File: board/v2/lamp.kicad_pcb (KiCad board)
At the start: 4 copper layers, 24 x 24 mm, 44 parts, among them J1 Conn_01x01_Female, J2 Conn_01x01_Female, J3 Conn_01x01_Female, J4 Conn_01x01_Female, J5 Conn_01x01_Female, J6 Conn_01x01_Female, J7 Conn_01x01_Female, U1 STM32F030F4P6, U2 LMV321, U3 MIC5205-3.3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

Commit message: hardware: Various fixes
* Fix component values
* Replace MIC5202 which wasn't ceramic-stable
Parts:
- R11: value 22k -> 8.2k
- R12: value 4.7k -> 2.2k
- R5: value 100k -> 120k
- R9: value 50k -> 10k
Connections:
- net Net-(TP1-Pad1) renamed /RESET
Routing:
- net Net-(R11-Pad2): track 12.5 -> 2.64 mm, vias 2 -> 0
- net /PWRGD: track 9.03 -> 0.00 mm, vias 2 -> 0
- net Net-(U1-Pad18): track 0.00 -> 7.06 mm
- net /RESET: track 5.54 -> 9.03 mm, vias 0 -> 2
- net /VBAT: track 8.99 -> 12.5 mm, vias 1 -> 2
- net Net-(D1-Pad2): track 2.18 -> 5.62 mm
- net Net-(R4-Pad2): track 5.81 -> 8.99 mm
- net Net-(C10-Pad1): track 2.64 -> 0.00 mm
- net Net-(R9-Pad2): track 8.17 -> 5.81 mm
- net Net-(U1-Pad2): track 0.00 -> 1.83 mm
- net Net-(C16-Pad1): track 7.06 -> 8.17 mm, vias 0 -> 1
- net Net-(C7-Pad1): track 1.83 -> 2.87 mm
- net Net-(J4-Pad1): track 2.87 -> 2.18 mm

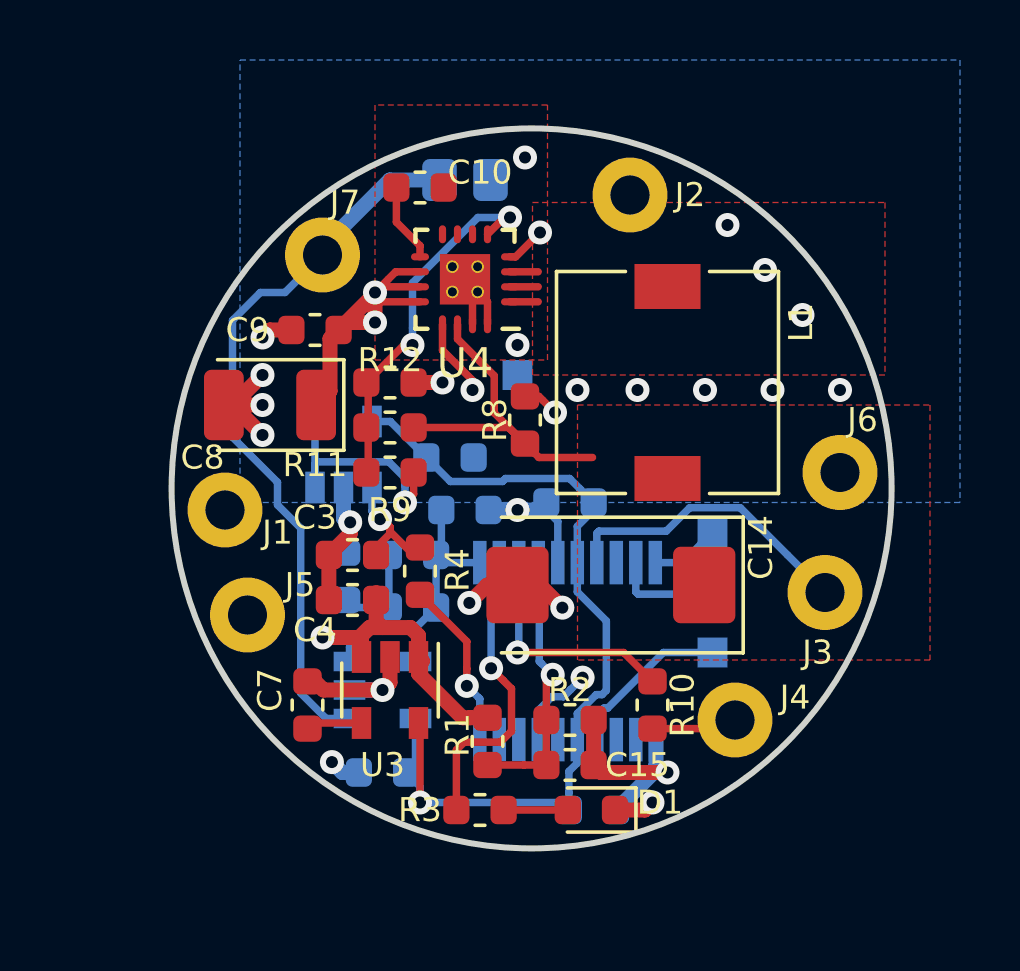
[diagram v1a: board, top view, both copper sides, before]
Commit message: board/v2: Various design changes
 * Switch from MIC5202 to LP2985 due to ceramic stability issues
   with former

 * Use TLV333 for op-amps for reduced power and offset

 * Move current sense amplifier next to sense resistor
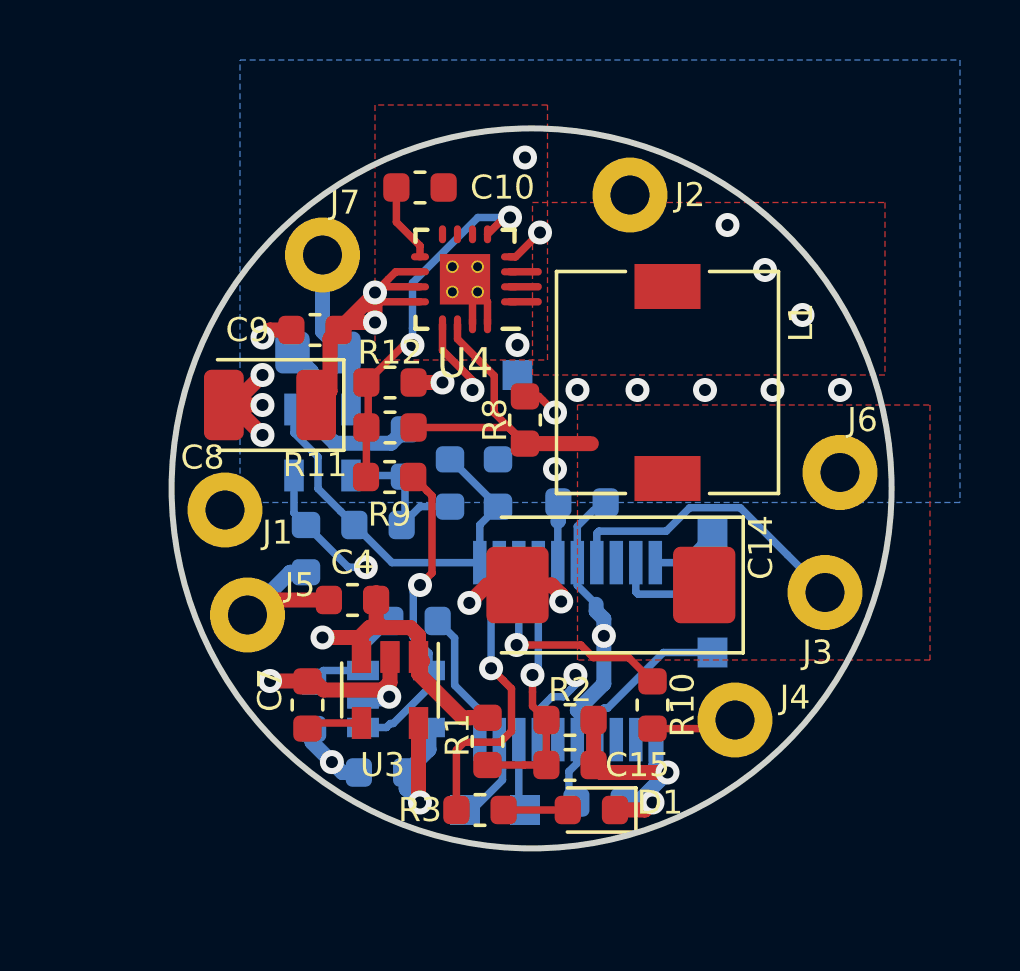
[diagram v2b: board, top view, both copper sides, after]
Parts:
- added TP5: Test_Point, TestPoint:TestPoint_Pad_1.0x1.0mm, B.Cu at (135.5, 94.5)
- added TP6: Test_Point, TestPoint:TestPoint_Pad_1.0x1.0mm, B.Cu at (133.5, 94.5)
- C3: value 1u -> 100n; moved to B.Cu
- C4: value 100n -> 4.7u
- C5: value 2.2u -> 4.7u
- C7: value 100n -> 470p
- R4: moved to B.Cu
- R5: value 120k -> 100k
- U2, U5: value LMV321 -> TLV333
- U3: value MIC5205-3.3 -> LP2985-33
- moved U2 8.49 mm to (128.8, 82.2), turned to 270 degrees
- moved U5 8.34 mm to (131.2, 90.8), turned to 0 degrees
- moved R13 7.55 mm to (128.6, 79.2), turned to 180 degrees
- moved C11 5.68 mm to (128.2, 85.8), turned to 270 degrees
- moved C3 5.19 mm to (128.4, 91.0), turned to 270 degrees
- moved R6 4.56 mm to (131.5, 82.6)
- moved R5 4.33 mm to (133.0, 83.6), turned to 90 degrees
- moved R4 1.67 mm to (131.8, 88.2), turned to 0 degrees
- moved C6 1.52 mm to (130.6, 85.0), turned to 180 degrees
- moved C16 1.42 mm to (134.6, 83.6), turned to 90 degrees
- moved C2 0.40 mm to (137.4, 84.2)
- moved C1 0.35 mm to (138.0, 94.2)
- moved R9 0.15 mm to (131.0, 83.4)
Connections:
- U1 pad 8: Net-(U1-Pad8) -> /DEBUG_TX
- U1 pad 9: Net-(U1-Pad9) -> /DEBUG_RX
- U2 pad 1: /ISENSE -> Net-(C16-Pad1)
- U2 pad 3: Net-(C6-Pad1) -> /ISENSE
- U2 pad 4: Net-(C16-Pad1) -> Net-(C6-Pad1)
- U5 pad 1: /SETPOINT -> Net-(R9-Pad2)
- U5 pad 3: Net-(R9-Pad2) -> /SETPOINT
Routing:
- net /ISENSE: track 24.4 -> 5.58 mm
- net Net-(R11-Pad2): track 2.64 -> 12.6 mm, vias 0 -> 2
- net +3V3: track 31.5 -> 41.3 mm, vias 1 -> 3
- net /PWRGD: track 0.00 -> 9.03 mm, vias 0 -> 2
- net Net-(U1-Pad18): track 7.06 -> 0.00 mm
- net GND: track 37.0 -> 43.4 mm
- net Net-(C16-Pad1): track 8.17 -> 13.9 mm, vias 1 -> 0
- net Net-(R9-Pad2): track 5.81 -> 10.8 mm
- net Net-(R4-Pad2): track 8.99 -> 4.65 mm, vias 1 -> 0
- net /VBAT: track 12.5 -> 8.98 mm, vias 2 -> 1
- net /RESET: track 9.03 -> 5.54 mm, vias 2 -> 0
- net Net-(D1-Pad2): track 5.62 -> 2.18 mm
- net /DEBUG_RX: track 0.00 -> 3.05 mm
- net Net-(C10-Pad1): track 0.00 -> 2.64 mm
- net /DEBUG_TX: track 0.00 -> 2.43 mm
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- added copper zone on In2.Cu, net GND

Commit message: board/v2: Use two-channel op-amp
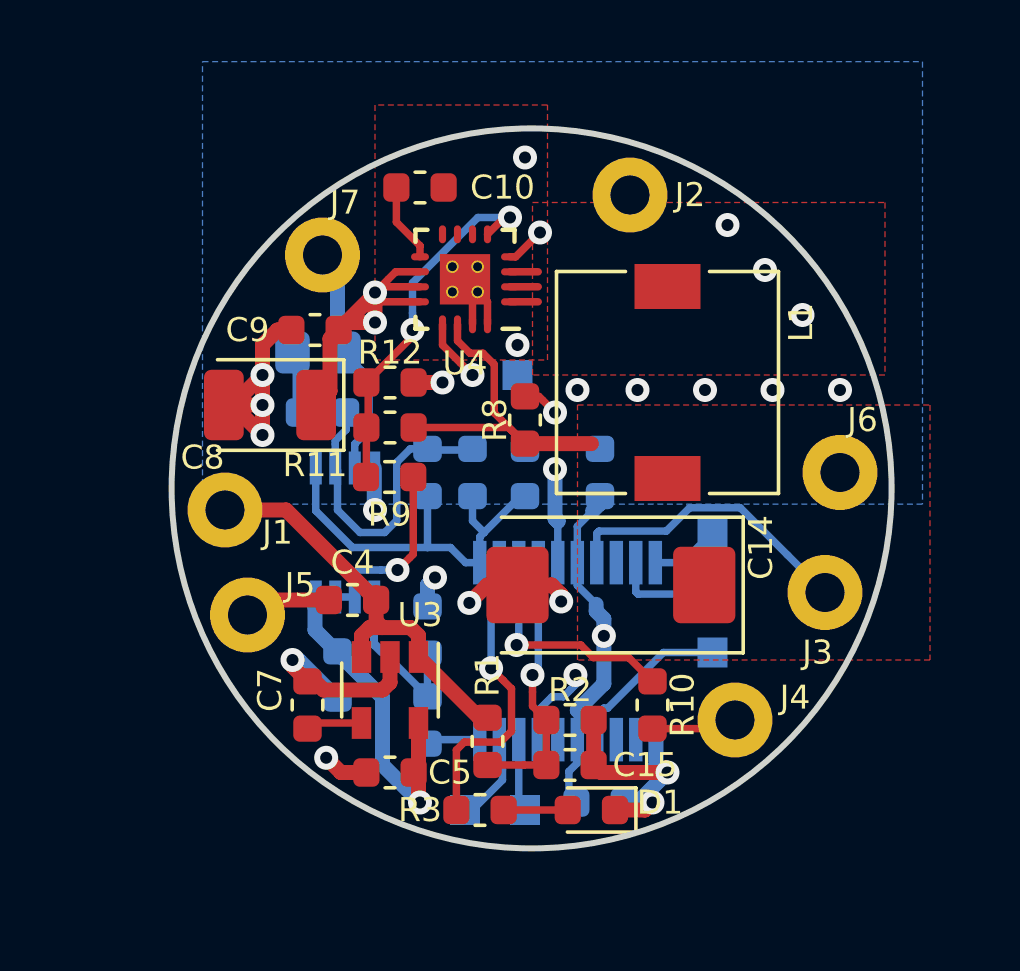
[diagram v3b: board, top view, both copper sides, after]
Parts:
- removed U5: TLV333, Package_TO_SOT_SMD:SOT-23-5
- C10: value 3.3n -> 4.7n
- C5: moved to F.Cu
- C7: value 470p -> 10n
- U2: value TLV333 -> TLV2333; footprint Package_TO_SOT_SMD:SOT-23-5 -> Package_SO:TSSOP-8_3x3mm_P0.65mm
- moved C3 4.60 mm to (132.2, 88.5), turned to 90 degrees
- moved C11 4.34 mm to (129.2, 90.0)
- moved R4 3.33 mm to (132.2, 91.5), turned to 270 degrees
- moved U2 3.09 mm to (129.5, 85.2)
- moved R6 3.06 mm to (128.8, 81.2), turned to 0 degrees
- moved C6 2.41 mm to (132.2, 83.2), turned to 270 degrees
- moved C2 1.17 mm to (138.0, 83.2), turned to 90 degrees
- moved C16 0.97 mm to (135.5, 83.2)
- moved R5 0.83 mm to (133.8, 83.2), turned to 270 degrees
- moved C5 0.25 mm to (131.0, 93.2)
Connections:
- U2 pad 2: GND -> Net-(C6-Pad1)
- U2 pad 4: Net-(C6-Pad1) -> GND
- U2 pad 5: +3V3 -> /SETPOINT
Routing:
- net +3V3: track 41.3 -> 33.8 mm, vias 3 -> 2
- net Net-(C6-Pad1): track 5.34 -> 10.5 mm
- net Net-(R9-Pad2): track 10.8 -> 6.23 mm
- net /VIN: track 22.7 -> 26.8 mm, vias 3 -> 2
- net /SETPOINT: track 3.88 -> 7.02 mm
- net /ISENSE: track 5.58 -> 7.98 mm
- net Net-(R4-Pad2): track 4.65 -> 2.41 mm
- net GND: track 43.4 -> 44.4 mm

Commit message: Hardware changes
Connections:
- net Net-(C16-Pad1) renamed /ISENSE_BUFD
- net Net-(R4-Pad2) renamed /SETPOINT_PWM

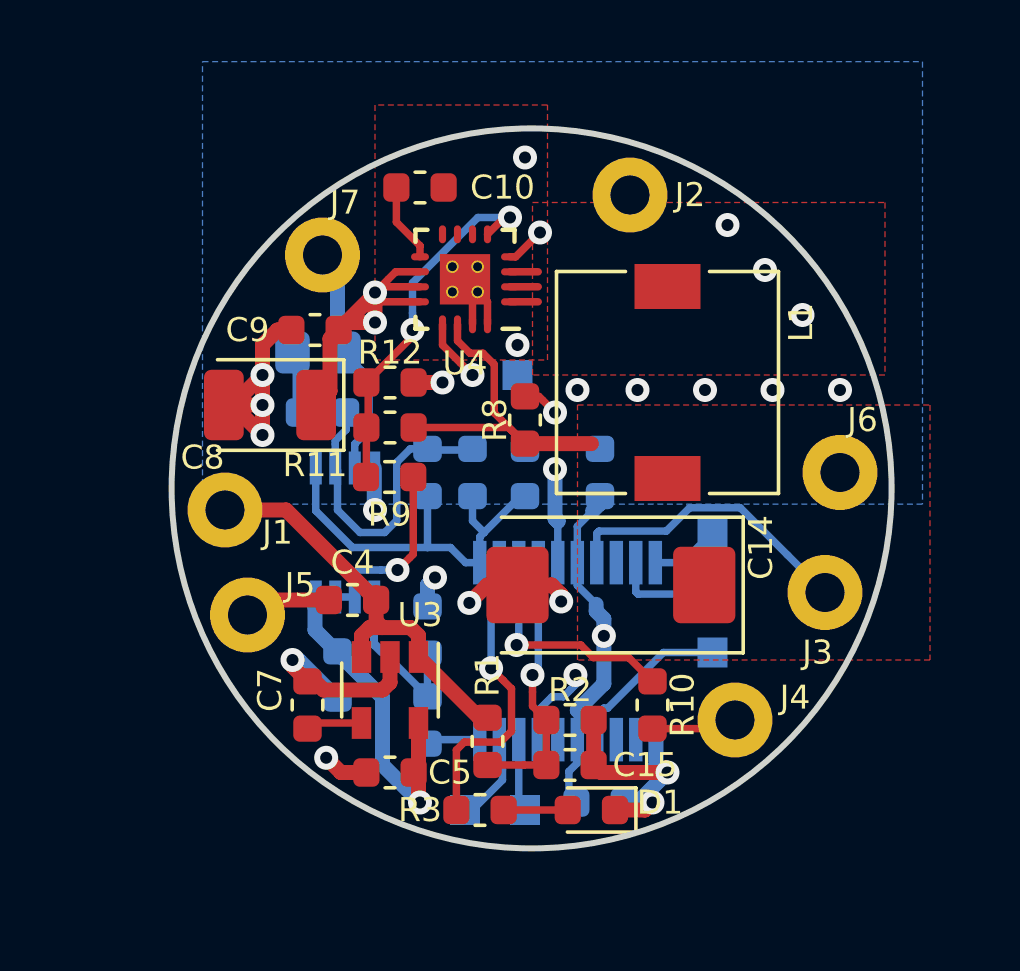
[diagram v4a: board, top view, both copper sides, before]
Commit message: board/v2: Move to STM32L041F6P7
This required only a small change in pinning which can be easily bodged
onto the existing boards.
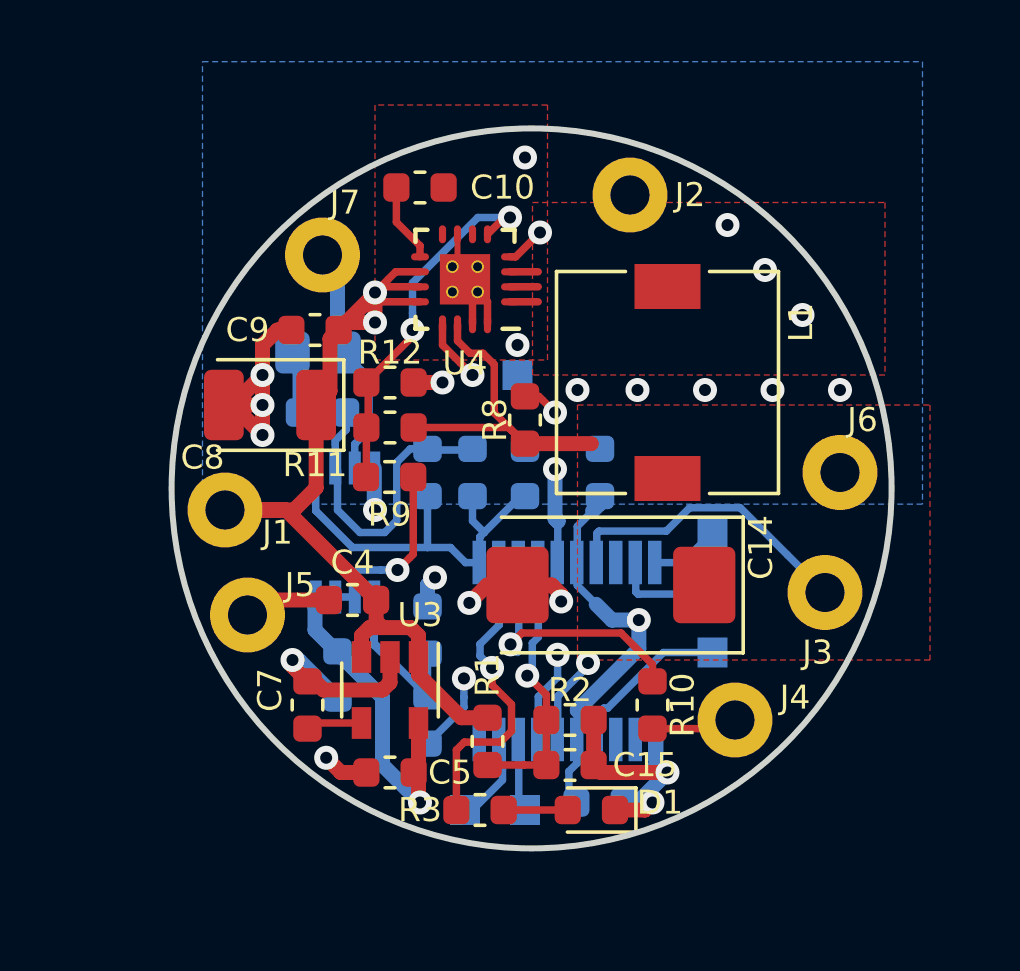
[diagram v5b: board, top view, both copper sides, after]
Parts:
- U1: value STM32F030F4P6 -> STM32L041F6Px
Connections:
- U1 pad 10: /SETPOINT_PWM -> Net-(U1-Pad10)
- U1 pad 6: Net-(U1-Pad6) -> /SETPOINT_PWM
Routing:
- net /SETPOINT_PWM: track 2.41 -> 10.6 mm, vias 0 -> 2
- net /VIN: track 26.8 -> 33.2 mm
- net +3V3: track 33.8 -> 37.5 mm
- net GND: track 44.4 -> 45.5 mm
- net /EN: track 16.7 -> 15.7 mm
- net /LED2: track 8.09 -> 9.09 mm
- net Net-(U1-Pad10): track 0.00 -> 0.61 mm
- added copper zone on In1.Cu, net /VIN
- removed copper zone on In2.Cu, net /VIN

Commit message: hardware: Kicad update
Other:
- net class Default removed
- net class Power removed

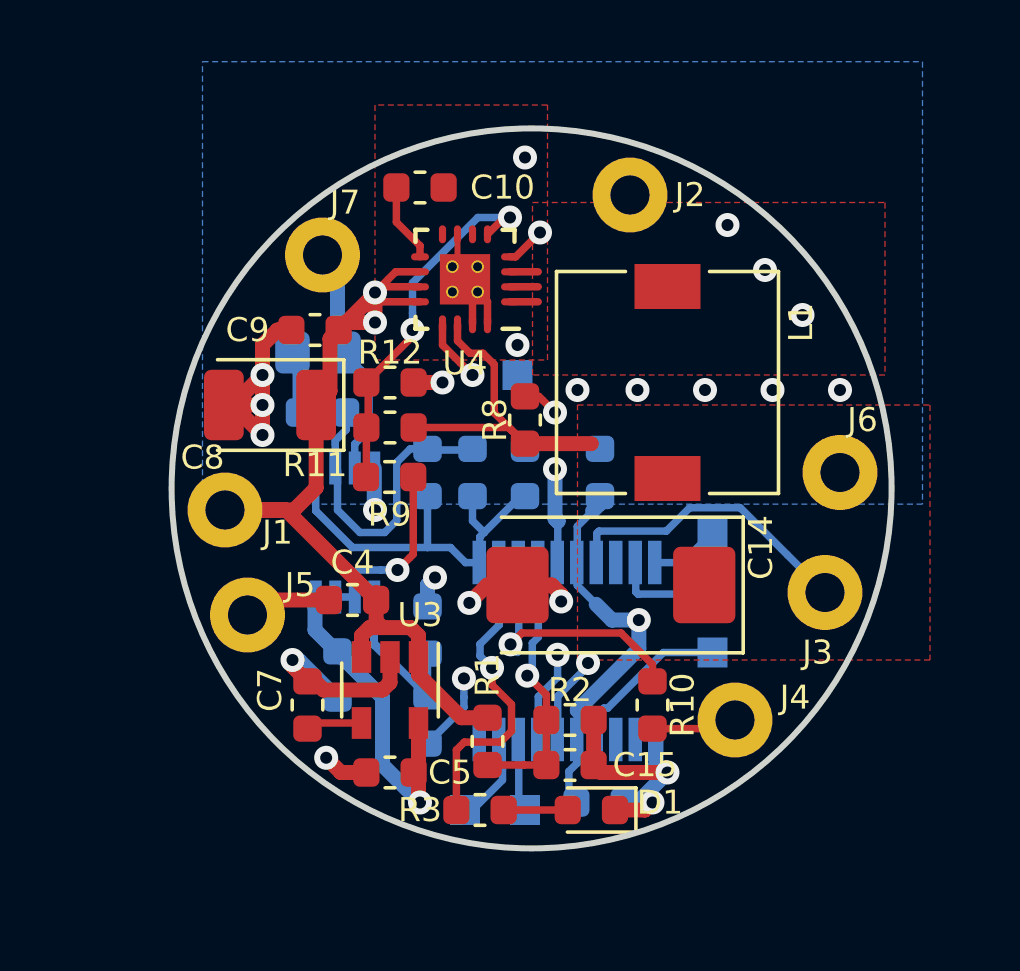
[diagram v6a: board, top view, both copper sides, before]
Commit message: hardware: Revision 3
 * Increase board size to 28mm diameter
 * Use proper 1.27 mm pin socket for debug
 * Move to STM32L051K MCU
 * Drop thermal cut-out
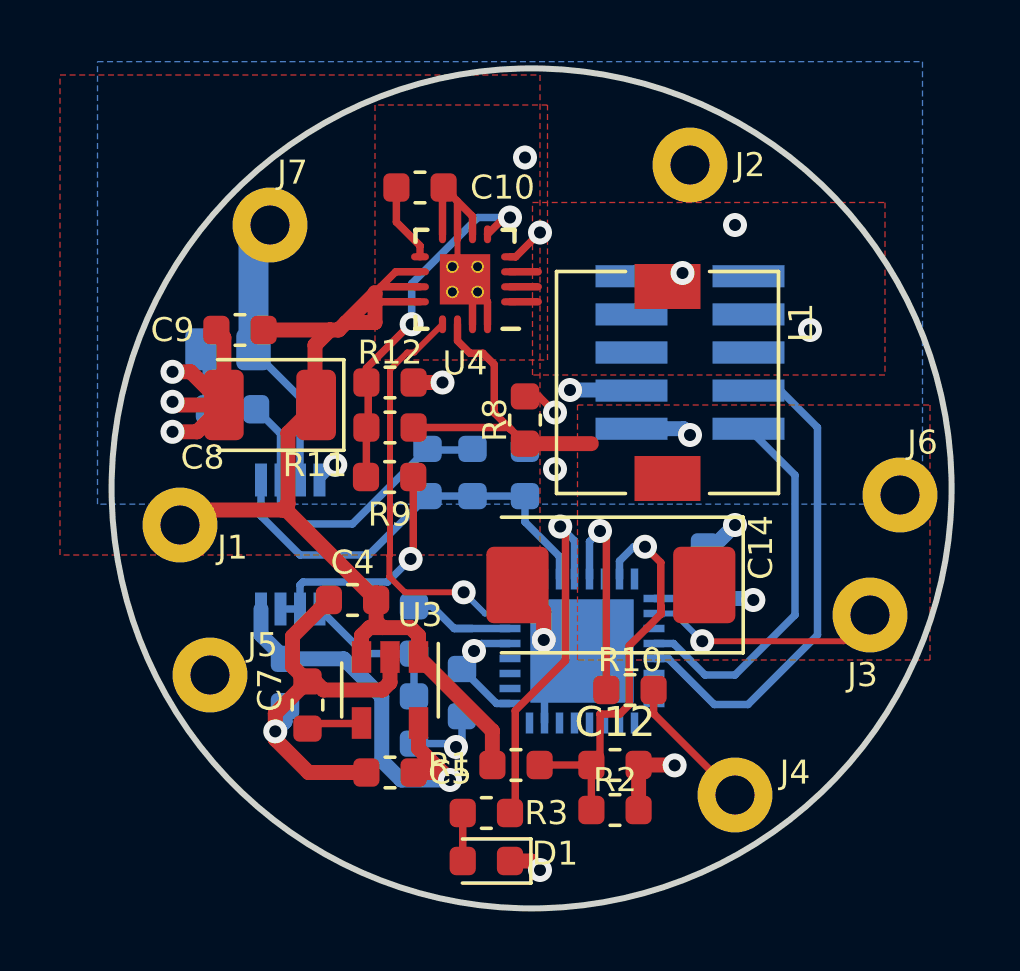
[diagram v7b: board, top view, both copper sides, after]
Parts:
- removed C15: 10n, Capacitor_SMD:C_0603_1608Metric
- removed TP1, TP2, TP3, TP4, TP5, TP6: Test_Point, TestPoint:TestPoint_Pad_1.0x1.0mm
- added C12: 10n, Capacitor_SMD:C_0603_1608Metric, F.Cu at (138.5, 93.0)
- added J8: Conn_ARM_JTAG_SWD_10, Connector_PinHeader_1.27mm:PinHeader_2x05_P1.27mm_Vertical_SMD, B.Cu at (141.0, 79.2)
- U1: value STM32L041F6Px -> STM32L051K8Ux; footprint Package_SO:TSSOP-20_4.4x6.5mm_P0.65mm -> Package_DFN_QFN:QFN-32-1EP_5x5mm_P0.5mm_EP3.45x3.45mm
- moved C2 8.66 mm to (133.4, 90.6), turned to -90 degrees
- moved C1 8.50 mm to (141.5, 86.5), turned to 90 degrees
- moved D1 3.89 mm to (134.2, 96.2)
- moved R2 3.35 mm to (138.5, 94.5)
- moved C3 3.03 mm to (131.8, 91.5), turned to -90 degrees
- moved R4 3.03 mm to (131.8, 88.5), turned to 90 degrees
- moved R13 3.00 mm to (125.6, 79.1)
- moved R6 3.00 mm to (125.8, 81.1)
- moved C9 2.50 mm to (126.0, 78.5)
- moved J4 2.50 mm to (142.5, 94.0)
- moved J5 2.36 mm to (125.0, 90.0)
- moved J2 2.24 mm to (141.0, 73.0)
- moved J6 2.14 mm to (148.0, 84.0)
- moved J7 2.02 mm to (127.0, 75.0)
- moved U2 1.87 mm to (127.7, 85.7)
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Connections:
- U1 pad 1: GND -> +3V3
- U1 pad 10: Net-(U1-Pad10) -> unconnected-(U1-Pad10)
- U1 pad 14: /VBAT -> unconnected-(U1-Pad14)
- U1 pad 15: GND -> /VBAT
- U1 pad 16: +3V3 -> unconnected-(U1-Pad16)
- U1 pad 17: /BTN -> +3V3
- U1 pad 18: Net-(U1-Pad18) -> /BTN
- U1 pad 19: /SWDIO -> unconnected-(U1-Pad19)
- U1 pad 2: Net-(U1-Pad2) -> unconnected-(U1-Pad2)
- U1 pad 20: /SWCLK -> /SWDIO
- U1 pad 3: Net-(U1-Pad3) -> unconnected-(U1-Pad3)
- U1 pad 8: /DEBUG_TX -> unconnected-(U1-Pad8)
- U1 pad 9: /DEBUG_RX -> unconnected-(U1-Pad9)
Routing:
- net /SWDCLK: track 0.00 -> 15.9 mm
- net +3V3: track 37.5 -> 22.8 mm, vias 2 -> 4
- net /SWDIO: track 3.59 -> 12.8 mm
- net /SETPOINT_PWM: track 10.6 -> 4.11 mm, vias 2 -> 0
- net GND: track 45.5 -> 51.3 mm, vias 23 -> 17
- net /RESET: track 5.54 -> 0.00 mm
- net /VBAT: track 9.12 -> 14.3 mm
- net /DEBUG_RX: track 3.05 -> 0.00 mm
- net Net-(J4-Pad1): track 2.87 -> 5.47 mm
- net /DEBUG_TX: track 2.43 -> 0.00 mm
- net /SWCLK: track 2.32 -> 0.00 mm
- net /BTN: track 10.1 -> 7.95 mm, vias 0 -> 1
- net /LED1: track 10.4 -> 12.5 mm
- net Net-(R9-Pad2): track 6.23 -> 8.27 mm
- net /EN: track 15.7 -> 13.8 mm, vias 2 -> 1
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- added copper zone on In2.Cu, net +3V3
- added copper zone on F.Cu, net /VIN
- removed copper zone on In1.Cu, net /VIN
- removed copper zone on In2.Cu, net GND
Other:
- board size 24 x 24 mm -> 28 x 28 mm
